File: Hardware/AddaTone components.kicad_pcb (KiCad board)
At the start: 2 copper layers, 60 x 110 mm, 82 parts, among them J1 SWD_Header, J2 Conn_01x20_Female, J3 Conn_01x20_Female, J8 Eurorack_16_pin_power, U1 STM32F446RETx, U2 ICE40UP5K-SG48ITR, U3 MCP6004, U4 PCM5100APW, U5 TL072, U6 LD1117S12TR, U7 LM1117-3.3, Y1 ECS-12MHz

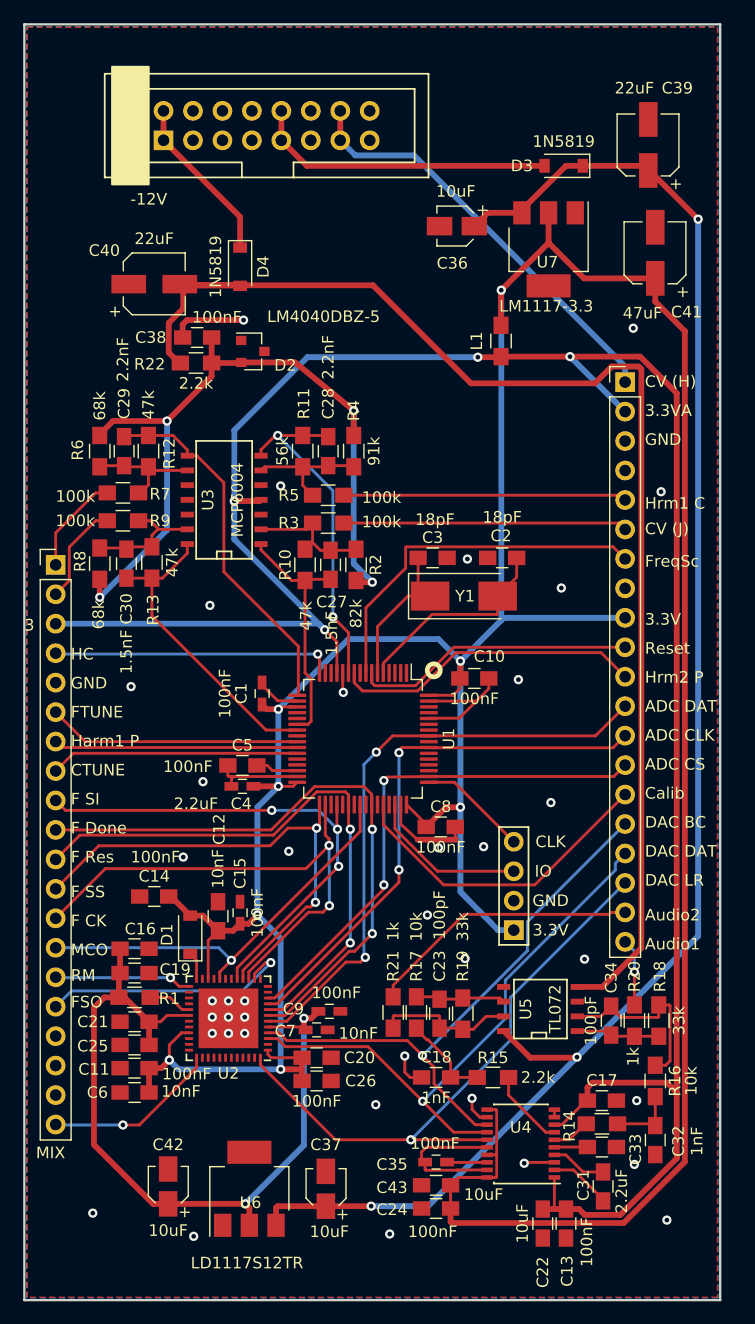
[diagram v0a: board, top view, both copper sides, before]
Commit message: Rough layout of controls PCB
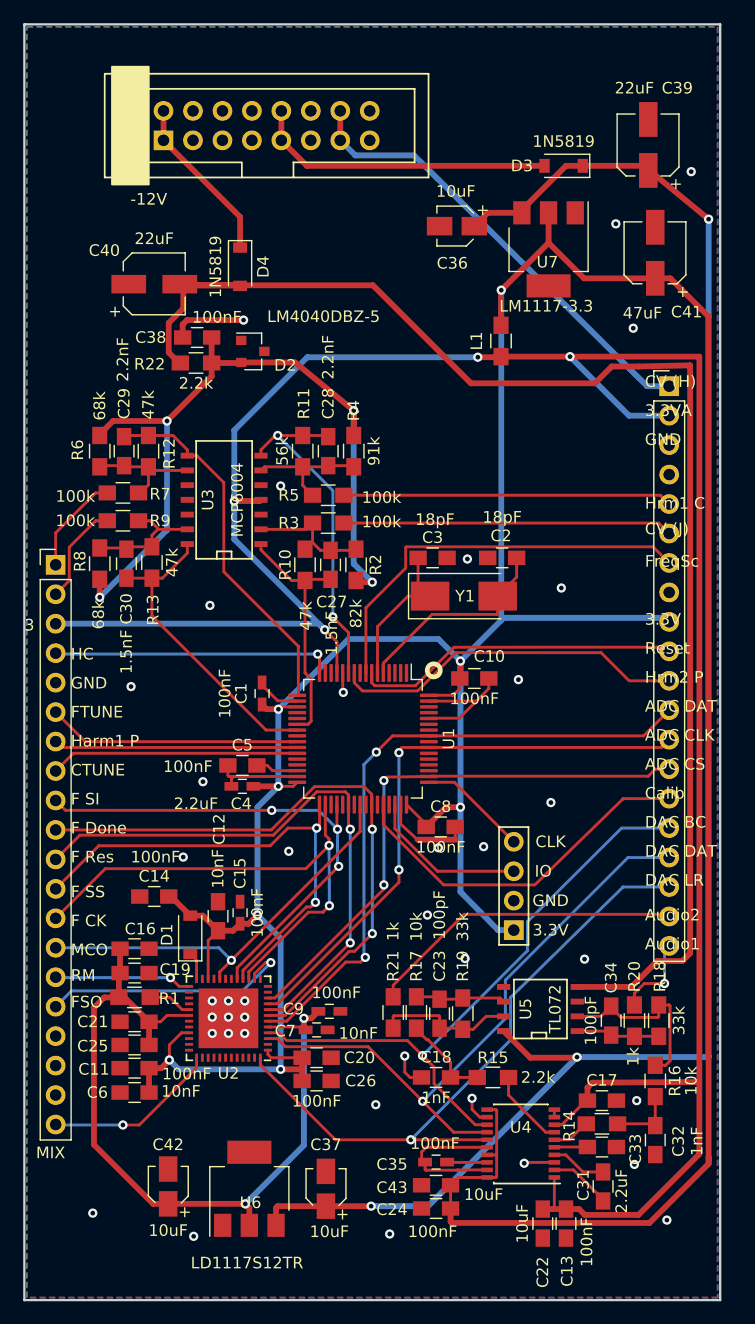
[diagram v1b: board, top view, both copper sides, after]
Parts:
- moved J3 3.82 mm to (155.6, 81.2)
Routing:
- net +3.3VA: track 194.7 -> 205.6 mm
- net VEE: track 113.1 -> 122.0 mm
- net VCCIO_0: track 316.3 -> 324.3 mm
- net VCC: track 141.6 -> 149.3 mm
- net RESET: track 24.2 -> 28.1 mm
- net FREQ_SC_POT: track 31.6 -> 35.6 mm
- net PITCH_CVIN: track 24.5 -> 28.4 mm
- net HARM1_CVIN: track 24.4 -> 28.4 mm
- net HARM2_POT: track 26.7 -> 30.7 mm
- net AUDIO2_OUT: track 23.6 -> 27.4 mm
- net ADC_Data: track 52.0 -> 55.7 mm
- net ADC_CS: track 44.7 -> 48.3 mm
- net DAC_BCLK: track 50.2 -> 53.9 mm
- net ADC_Clock: track 47.2 -> 50.9 mm
- net DAC_LRCLK: track 52.6 -> 56.2 mm
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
